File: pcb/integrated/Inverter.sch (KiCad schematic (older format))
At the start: 17 parts, among them J10001 Conn_01x02_Female, Q10001 F423MR12W1M1B11BOMA1

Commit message: revised power input schematic
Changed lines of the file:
@@
 U 5D640666
 F0 "Gate Drive 2" 50
-F1 "GateDrive.sch" 50
+F1 "GateDrive_alt.sch" 50
 F2 "Gate" I R 1800 3750 50
 F3 "Source" I R 1800 3950 50
@@
 Text GLabel 1650 1450 0    50   Input ~ 0
 TEMP_B
+Text GLabel 5350 1150 0    50   Input ~ 0
+VBUS
 $EndSCHEMATC

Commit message: routing, all componens placed on PCB
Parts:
- removed C10006: 33n, Capacitor_THT:C_Rect_L18.0mm_W7.0mm_P15.00mm_FKS3_FKP3, symbol Device:C
- removed J10001: Conn_01x02_Female, wbraun_smd:Anderson_PP45_2x1, symbol Connector:Conn_01x02_Female
- removed R10005, R10006: R, Resistor_SMD:R_0805_2012Metric, symbol Device:R
- removed R10008: R, Resistor_SMD:R_0603_1608Metric, symbol Device:R
- added J10001, J10002: Conn_01x01_Female, wbraun_smd:7693-term, symbol Connector:Conn_01x01_Female
- R10007: footprint Resistor_SMD:R_0603_1608Metric -> Resistor_SMD:R_0805_2012Metric
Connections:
- net Out2: now also J10002.1 (Pin_1)
- net VBUS_SENSE: now also R10004.2, R10007.1
- net SW_NODE renamed Out1
- net Out1: now also J10001.1 (Pin_1)
- net TEMP_A renamed GND
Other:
- moved on the sheet: R10007
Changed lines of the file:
@@
-$EndComp
-$Comp
-L Device:R R10005
-U 1 1 5D8CBCDF
-P 7850 3550
-F 0 "R10005" H 7920 3596 50  0000 L CNN
-F 1 "R" H 7920 3505 50  0000 L CNN
-F 2 "Resistor_SMD:R_0805_2012Metric" V 7780 3550 50  0001 C CNN
-F 3 "~" H 7850 3550 50  0001 C CNN
-	1    7850 3550
-	1    0    0    -1
-$EndComp
-$Comp
-L Device:R R10006
-U 1 1 5D8CBD1D
-P 7850 3950
-F 0 "R10006" H 7920 3996 50  0000 L CNN
-F 1 "R" H 7920 3905 50  0000 L CNN
-F 2 "Resistor_SMD:R_0805_2012Metric" V 7780 3950 50  0001 C CNN
-F 3 "~" H 7850 3950 50  0001 C CNN
-	1    7850 3950
-	1    0    0    -1
 $EndComp
 $Comp
 L Device:R R10007
 U 1 1 5D8CBD59
-P 7850 4450
-F 0 "R10007" H 7920 4496 50  0000 L CNN
-F 1 "R" H 7920 4405 50  0000 L CNN
-F 2 "Resistor_SMD:R_0603_1608Metric" V 7780 4450 50  0001 C CNN
-F 3 "~" H 7850 4450 50  0001 C CNN
-	1    7850 4450
+P 7850 3750
+F 0 "R10007" H 7920 3796 50  0000 L CNN
+F 1 "R" H 7920 3705 50  0000 L CNN
+F 2 "Resistor_SMD:R_0805_2012Metric" V 7780 3750 50  0001 C CNN
+F 3 "~" H 7850 3750 50  0001 C CNN
+	1    7850 3750
 	1    0    0    -1
 $EndComp
-$Comp
-L Device:R R10008
-U 1 1 5D8CBD9B
-P 8300 4200
-F 0 "R10008" V 8507 4200 50  0000 C CNN
-F 1 "R" V 8416 4200 50  0000 C CNN
-F 2 "Resistor_SMD:R_0603_1608Metric" V 8230 4200 50  0001 C CNN
-F 3 "~" H 8300 4200 50  0001 C CNN
-	1    8300 4200
-	0    -1   -1   0
-$EndComp
+Connection ~ 7850 3500
 Wire Wire Line
-	7850 4100 7850 4200
-Wire Wire Line
-	7850 4200 8150 4200
-Connection ~ 7850 4200
-Wire Wire Line
-	7850 4200 7850 4300
+	7850 3500 7850 3600
 Wire Wire Line
 	7850 2100 7850 2200
@@
 Wire Wire Line
 	7850 2900 7850 3000
-Wire Wire Line
-	7850 3300 7850 3400
-Wire Wire Line
-	7850 3700 7850 3800
 $Comp
 L power:GNDPWR #PWR010004
 U 1 1 5D8D0EF1
-P 7850 4850
-F 0 "#PWR010004" H 7850 4650 50  0001 C CNN
-F 1 "GNDPWR" H 7854 4696 50  0000 C CNN
-F 2 "" H 7850 4800 50  0001 C CNN
-F 3 "" H 7850 4800 50  0001 C CNN
-	1    7850 4850
+P 7850 4150
+F 0 "#PWR010004" H 7850 3950 50  0001 C CNN
+F 1 "GNDPWR" H 7854 3996 50  0000 C CNN
+F 2 "" H 7850 4100 50  0001 C CNN
+F 3 "" H 7850 4100 50  0001 C CNN
+	1    7850 4150
 	1    0    0    -1
 $EndComp
@@
 Wire Wire Line
 	7850 1700 7850 1800
-Wire Wire Line
-	8450 4200 8600 4200
 $Comp
 L Device:C C10005
@@
 $Comp
 L Device:C C?
-U 1 1 5D747C8C
-P 5800 1350
-AR Path="/5D33C751/5D747C8C" Ref="C?"  Part="1"
-AR Path="/5D688380/5D747C8C" Ref="C?"  Part="1"
-AR Path="/5D68A538/5D747C8C" Ref="C10006"  Part="1"
-F 0 "C10006" H 5915 1396 50  0000 L CNN
-F 1 "33n" H 5915 1305 50  0000 L CNN
-F 2 "Capacitor_THT:C_Rect_L18.0mm_W7.0mm_P15.00mm_FKS3_FKP3" H 5838 1200 50  0001 C CNN
-F 3 "~" H 5800 1350 50  0001 C CNN
-	1    5800 1350
-	1    0    0    -1
-$EndComp
-$Comp
-L Device:C C?
 U 1 1 5D747C93
 P 5800 1800
@@
 $EndComp
 Wire Wire Line
-	5800 1150 5800 1200
-Wire Wire Line
-	5800 1500 5800 1550
-Wire Wire Line
 	5800 1550 5600 1550
 Wire Wire Line
 	5600 1550 5600 1650
-Connection ~ 5800 1550
 Wire Wire Line
 	5800 1550 5800 1650
@@
 Wire Wire Line
 	5350 1300 5350 1150
-Wire Wire Line
-	5350 1150 5800 1150
 Connection ~ 4950 1300
 Wire Wire Line
@@
 	5800 2000 5800 1950
 Connection ~ 4950 1750
-$Comp
-L Connector:Conn_01x02_Female J10001
-U 1 1 5D780C25
-P 5350 4050
-F 0 "J10001" H 5377 4026 50  0000 L CNN
-F 1 "Conn_01x02_Female" H 5377 3935 50  0000 L CNN
-F 2 "wbraun_smd:Anderson_PP45_2x1" H 5350 4050 50  0001 C CNN
-F 3 "~" H 5350 4050 50  0001 C CNN
-	1    5350 4050
-	1    0    0    1
-$EndComp
-Wire Wire Line
-	2750 3450 3000 3450
 Text Label 3050 3450 0    50   ~ 0
 Out1
 Text Label 2850 5500 0    50   ~ 0
 Out2
-Text GLabel 3050 3250 2    50   Input ~ 0
-SW_NODE
-Wire Wire Line
-	3050 3250 3000 3250
-Wire Wire Line
-	3000 3250 3000 3450
-Connection ~ 3000 3450
-Wire Wire Line
-	3000 3450 3050 3450
-Text Label 5050 3950 2    50   ~ 0
-Out1
-Text Label 5050 4050 2    50   ~ 0
-Out2
-Wire Wire Line
-	5050 3950 5150 3950
-Wire Wire Line
-	5050 4050 5150 4050
-Text GLabel 8600 4200 2    50   Input ~ 0
+Text GLabel 8300 3500 2    50   Input ~ 0
 VBUS_SENSE
 Wire Wire Line
-	7850 4600 7850 4850
+	7850 3900 7850 4150
 Wire Wire Line
 	1750 1050 1650 1050
 Wire Wire Line
 	1750 1450 1650 1450
-Text GLabel 1650 1050 0    50   Input ~ 0
-TEMP_A
 Text GLabel 1650 1450 0    50   Input ~ 0
 TEMP_B
 Text GLabel 5350 1150 0    50   Input ~ 0
 VBUS
+$Comp
+L Connector:Conn_01x01_Female J10001
+U 1 1 5DD3543B
+P 5100 3650
+F 0 "J10001" H 5128 3676 50  0000 L CNN
+F 1 "Conn_01x01_Female" H 5128 3585 50  0000 L CNN
+F 2 "wbraun_smd:7693-term" H 5100 3650 50  0001 C CNN
+F 3 "~" H 5100 3650 50  0001 C CNN
+	1    5100 3650
+	1    0    0    -1
+$EndComp
+$Comp
+L Connector:Conn_01x01_Female J10002
+U 1 1 5DD3590B
+P 5100 4000
+F 0 "J10002" H 5128 4026 50  0000 L CNN
+F 1 "Conn_01x01_Female" H 5128 3935 50  0000 L CNN
+F 2 "wbraun_smd:7693-term" H 5100 4000 50  0001 C CNN
+F 3 "~" H 5100 4000 50  0001 C CNN
+	1    5100 4000
+	1    0    0    -1
+$EndComp
+Text Label 4900 3650 2    50   ~ 0
+Out1
+Text Label 4900 4000 2    50   ~ 0
+Out2
+Wire Wire Line
+	2750 3450 3050 3450
+Wire Wire Line
+	7850 3300 7850 3500
+Wire Wire Line
+	7850 3500 8300 3500
+$Comp
+L power:GND #PWR0148
+U 1 1 5DDE3636
+P 1650 1050
+F 0 "#PWR0148" H 1650 800 50  0001 C CNN
+F 1 "GND" H 1655 877 50  0000 C CNN
+F 2 "" H 1650 1050 50  0001 C CNN
+F 3 "" H 1650 1050 50  0001 C CNN
+	1    1650 1050
+	1    0    0    -1
+$EndComp
+Text GLabel 1500 1050 0    50   Input ~ 0
+GND
+Wire Wire Line
+	1500 1050 1650 1050
+Connection ~ 1650 1050
 $EndSCHEMATC

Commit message: redid power planes
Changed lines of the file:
@@
 	1500 1050 1650 1050
 Connection ~ 1650 1050
+Text GLabel 900  3100 0    50   Input ~ 0
+GATE1
+Text GLabel 900  3850 0    50   Input ~ 0
+GATE2
+Text GLabel 1000 5250 0    50   Input ~ 0
+GATE3
+Text GLabel 1000 6000 0    50   Input ~ 0
+GATE4
+Wire Wire Line
+	900  3100 1000 3100
+Wire Wire Line
+	900  3850 1000 3850
+Wire Wire Line
+	1000 5250 1100 5250
+Wire Wire Line
+	1000 6000 1100 6000
 $EndSCHEMATC

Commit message: PCB routing finihsed, ready for design review
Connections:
- net GND renamed TEMP_A
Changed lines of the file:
@@
 	7850 3900 7850 4150
-Wire Wire Line
-	1750 1050 1650 1050
 Wire Wire Line
 	1750 1450 1650 1450
@@
 Wire Wire Line
 	7850 3500 8300 3500
-$Comp
-L power:GND #PWR0148
-U 1 1 5DDE3636
-P 1650 1050
-F 0 "#PWR0148" H 1650 800 50  0001 C CNN
-F 1 "GND" H 1655 877 50  0000 C CNN
-F 2 "" H 1650 1050 50  0001 C CNN
-F 3 "" H 1650 1050 50  0001 C CNN
-	1    1650 1050
-	1    0    0    -1
-$EndComp
-Text GLabel 1500 1050 0    50   Input ~ 0
-GND
-Wire Wire Line
-	1500 1050 1650 1050
-Connection ~ 1650 1050
 Text GLabel 900  3100 0    50   Input ~ 0
 GATE1
@@
 Wire Wire Line
 	1000 6000 1100 6000
+Wire Wire Line
+	1500 1050 1750 1050
+Text GLabel 1500 1050 0    50   Input ~ 0
+TEMP_A
 $EndSCHEMATC

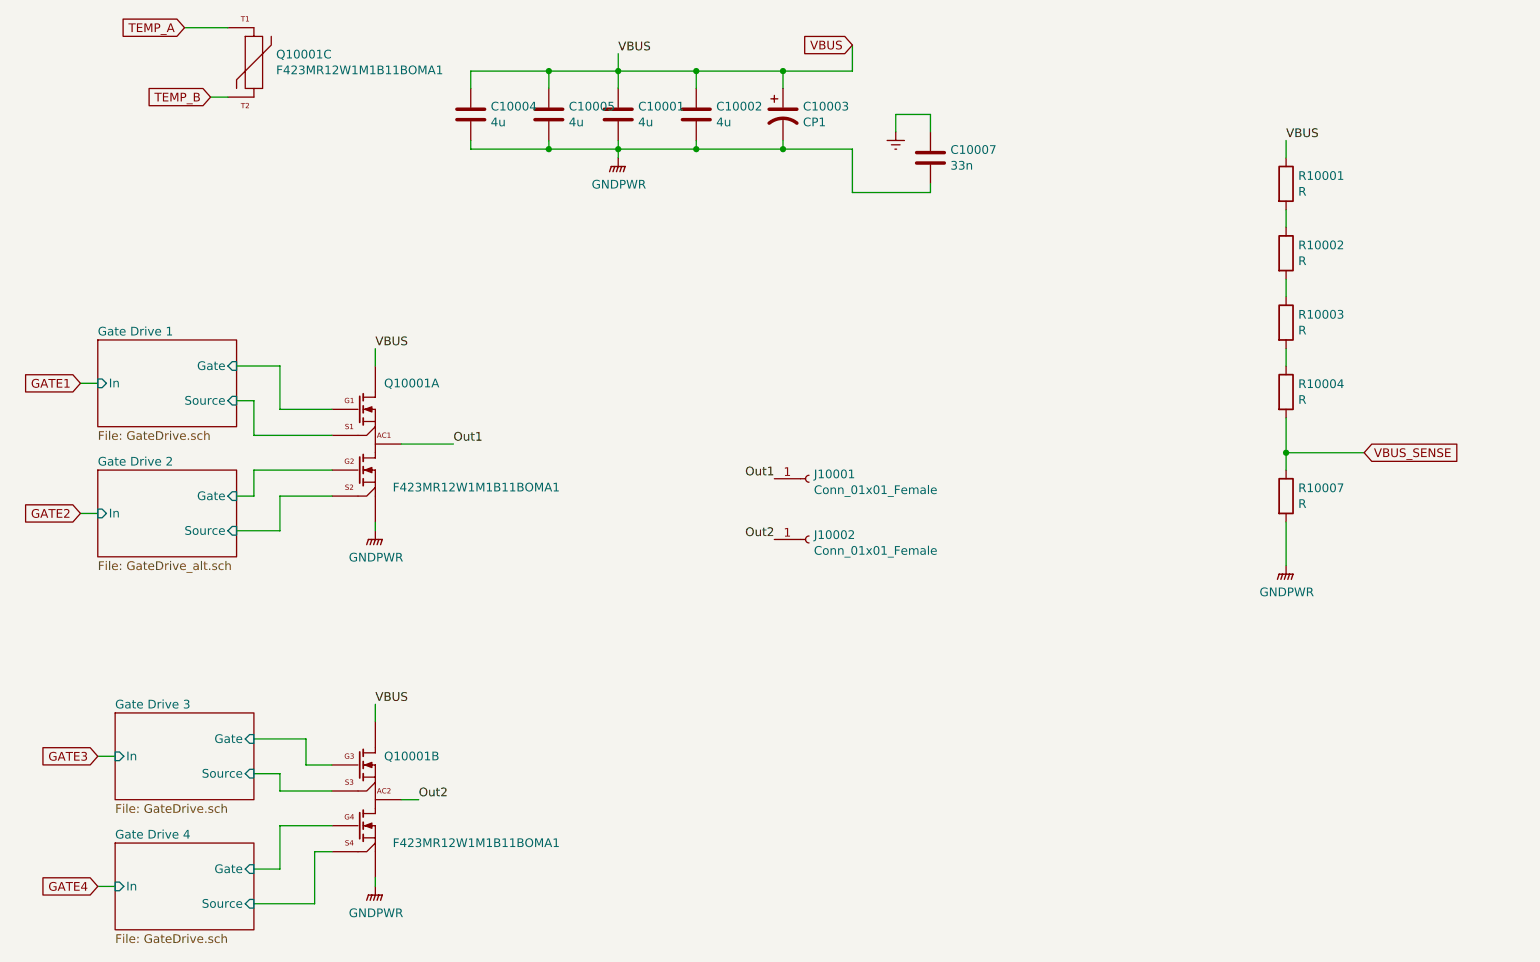
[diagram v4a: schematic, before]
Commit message: updated component values for schematic
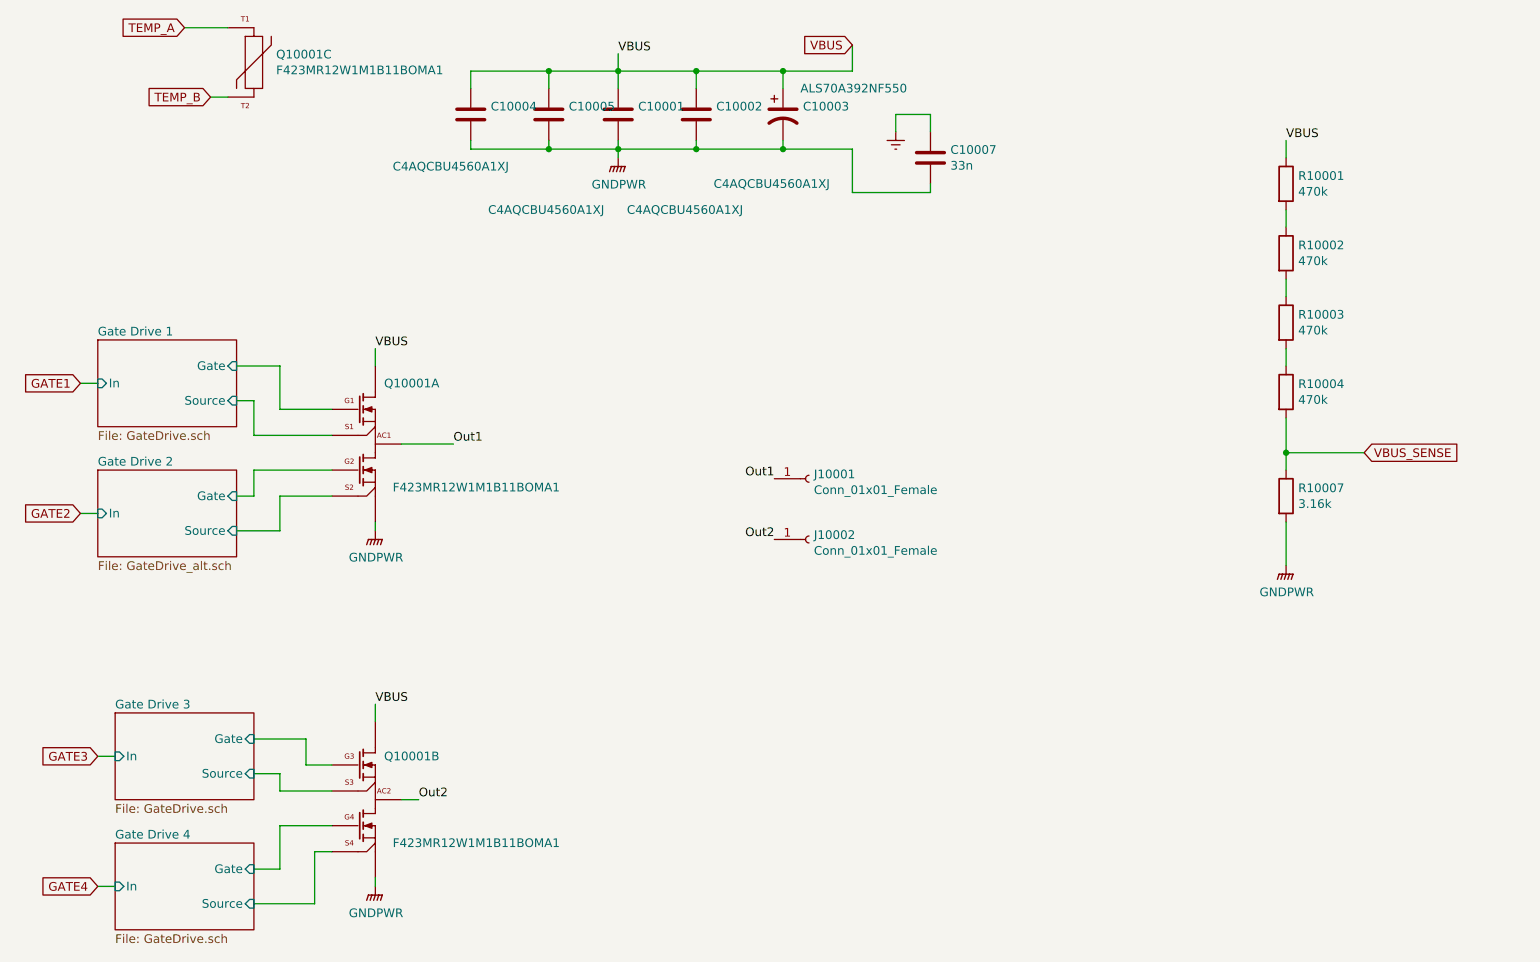
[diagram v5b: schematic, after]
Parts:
- C10001, C10002, C10004, C10005: value 4u -> C4AQCBU4560A1XJ
- C10003: value CP1 -> ALS70A392NF550
- R10001, R10002, R10003, R10004: value R -> 470k
- R10007: value R -> 3.16k
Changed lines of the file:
@@
 EESchema Schematic File Version 4
 LIBS:integrated-cache
-EELAYER 30 0
+EELAYER 26 0
 EELAYER END
 $Descr A4 11693 8268
@@
 P 4000 1550
 F 0 "C10001" H 4115 1596 50  0000 L CNN
-F 1 "4u" H 4115 1505 50  0000 L CNN
+F 1 "C4AQCBU4560A1XJ" H 4050 1000 50  0000 L CNN
 F 2 "Capacitor_THT:C_Rect_L31.5mm_W13.0mm_P27.50mm_MKS4" H 4038 1400 50  0001 C CNN
 F 3 "~" H 4000 1550 50  0001 C CNN
@@
 P 4450 1550
 F 0 "C10002" H 4565 1596 50  0000 L CNN
-F 1 "4u" H 4565 1505 50  0000 L CNN
+F 1 "C4AQCBU4560A1XJ" H 4550 1150 50  0000 L CNN
 F 2 "Capacitor_THT:C_Rect_L31.5mm_W13.0mm_P27.50mm_MKS4" H 4488 1400 50  0001 C CNN
 F 3 "~" H 4450 1550 50  0001 C CNN
@@
 P 4950 1550
 F 0 "C10003" H 5065 1596 50  0000 L CNN
-F 1 "CP1" H 5065 1505 50  0000 L CNN
+F 1 "ALS70A392NF550" H 5050 1700 50  0000 L CNN
 F 2 "wbraun_smd:CAP_77mm_stud_horizontal" H 4950 1550 50  0001 C CNN
 F 3 "~" H 4950 1550 50  0001 C CNN
@@
 P 7850 1950
 F 0 "R10001" H 7920 1996 50  0000 L CNN
-F 1 "R" H 7920 1905 50  0000 L CNN
+F 1 "470k" H 7920 1905 50  0000 L CNN
 F 2 "Resistor_SMD:R_0805_2012Metric" V 7780 1950 50  0001 C CNN
 F 3 "~" H 7850 1950 50  0001 C CNN
@@
 P 7850 2350
 F 0 "R10002" H 7920 2396 50  0000 L CNN
-F 1 "R" H 7920 2305 50  0000 L CNN
+F 1 "470k" H 7920 2305 50  0000 L CNN
 F 2 "Resistor_SMD:R_0805_2012Metric" V 7780 2350 50  0001 C CNN
 F 3 "~" H 7850 2350 50  0001 C CNN
@@
 P 7850 2750
 F 0 "R10003" H 7920 2796 50  0000 L CNN
-F 1 "R" H 7920 2705 50  0000 L CNN
+F 1 "470k" H 7920 2705 50  0000 L CNN
 F 2 "Resistor_SMD:R_0805_2012Metric" V 7780 2750 50  0001 C CNN
 F 3 "~" H 7850 2750 50  0001 C CNN
@@
 P 7850 3150
 F 0 "R10004" H 7920 3196 50  0000 L CNN
-F 1 "R" H 7920 3105 50  0000 L CNN
+F 1 "470k" H 7920 3105 50  0000 L CNN
 F 2 "Resistor_SMD:R_0805_2012Metric" V 7780 3150 50  0001 C CNN
 F 3 "~" H 7850 3150 50  0001 C CNN
@@
 P 7850 3750
 F 0 "R10007" H 7920 3796 50  0000 L CNN
-F 1 "R" H 7920 3705 50  0000 L CNN
+F 1 "3.16k" H 7920 3705 50  0000 L CNN
 F 2 "Resistor_SMD:R_0805_2012Metric" V 7780 3750 50  0001 C CNN
 F 3 "~" H 7850 3750 50  0001 C CNN
@@
 P 3600 1550
 F 0 "C10005" H 3715 1596 50  0000 L CNN
-F 1 "4u" H 3715 1505 50  0000 L CNN
+F 1 "C4AQCBU4560A1XJ" H 3250 1000 50  0000 L CNN
 F 2 "Capacitor_THT:C_Rect_L31.5mm_W13.0mm_P27.50mm_MKS4" H 3638 1400 50  0001 C CNN
 F 3 "~" H 3600 1550 50  0001 C CNN
@@
 P 3150 1550
 F 0 "C10004" H 3265 1596 50  0000 L CNN
-F 1 "4u" H 3265 1505 50  0000 L CNN
+F 1 "C4AQCBU4560A1XJ" H 2700 1250 50  0000 L CNN
 F 2 "Capacitor_THT:C_Rect_L31.5mm_W13.0mm_P27.50mm_MKS4" H 3188 1400 50  0001 C CNN
 F 3 "~" H 3150 1550 50  0001 C CNN
